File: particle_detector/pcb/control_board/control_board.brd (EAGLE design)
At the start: 64 x 32 mm, 35 parts, among them IC1 LT1807R, IC2 TLV3501, IC3 LT3461, IC4 TEENSY 3.2

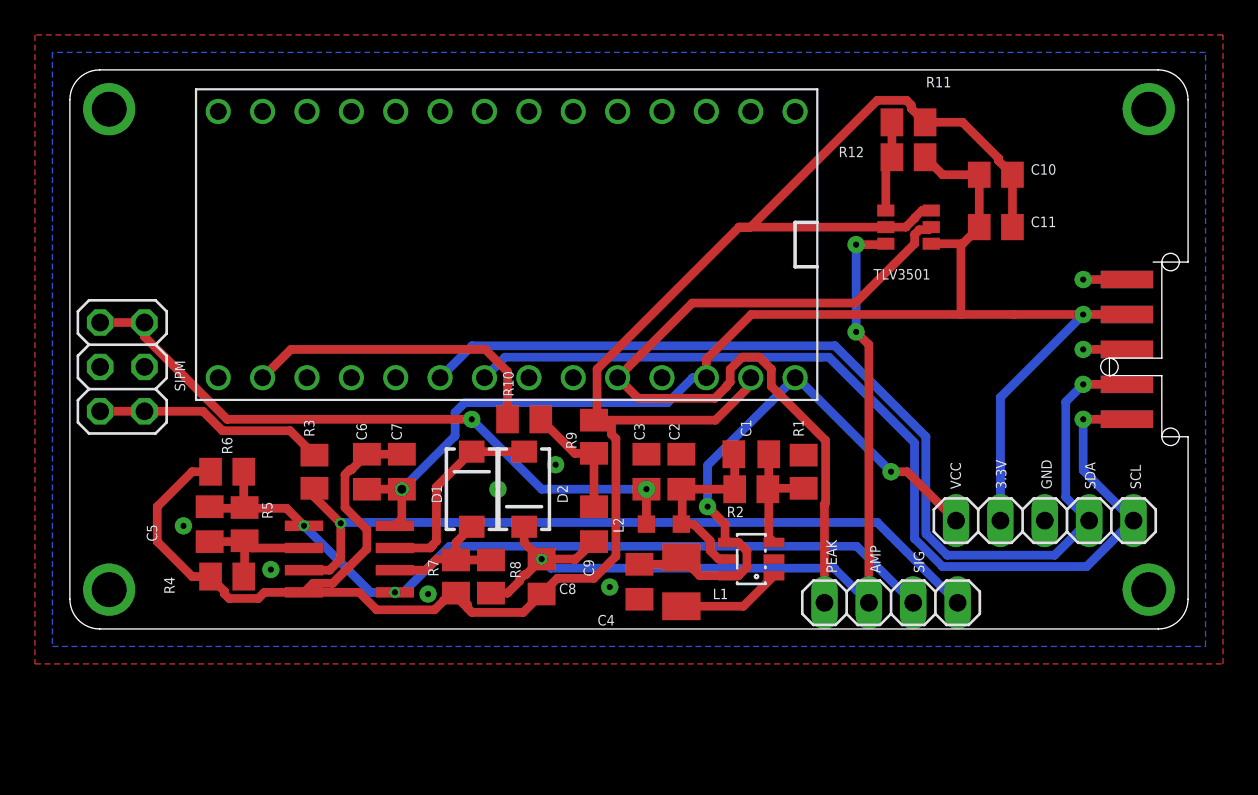
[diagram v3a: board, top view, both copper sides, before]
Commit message: remove VCC traces to DC-DC booster; 3.3V traces remain unrouted
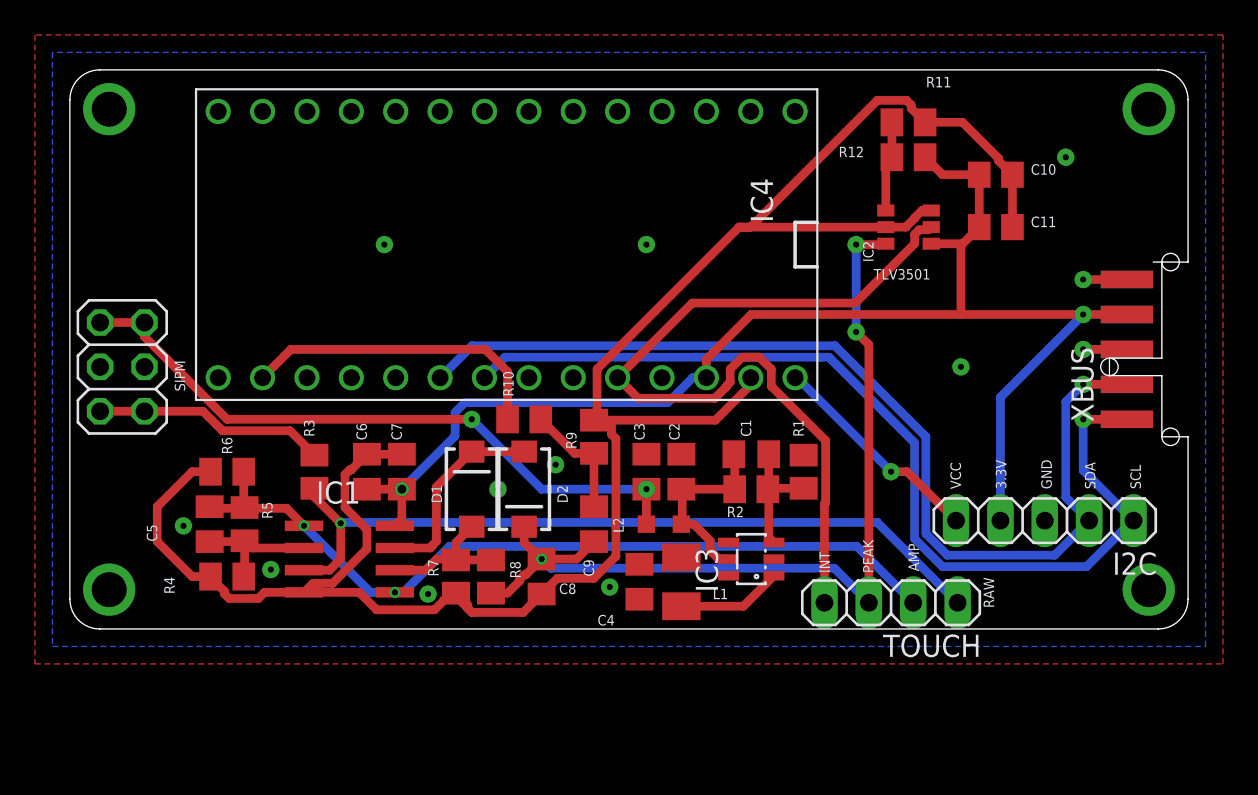
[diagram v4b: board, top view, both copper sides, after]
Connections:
- net 3.3V: now also C4.1, IC3.4, IC3.6, L1.1
- net VCC: no longer C4.1, IC3.4, IC3.6, L1.1
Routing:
- net VCC: track 33.7 -> 12.6 mm, vias 2 -> 1
- net 3.3V: track 78.8 -> 79.4 mm
- net GND: vias 11 -> 15
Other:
- board text added: "INT"
- board text added: "RAW"
- board text removed: "SIG"

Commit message: adjust comparator footprint; route 3.3V traces. send to fab
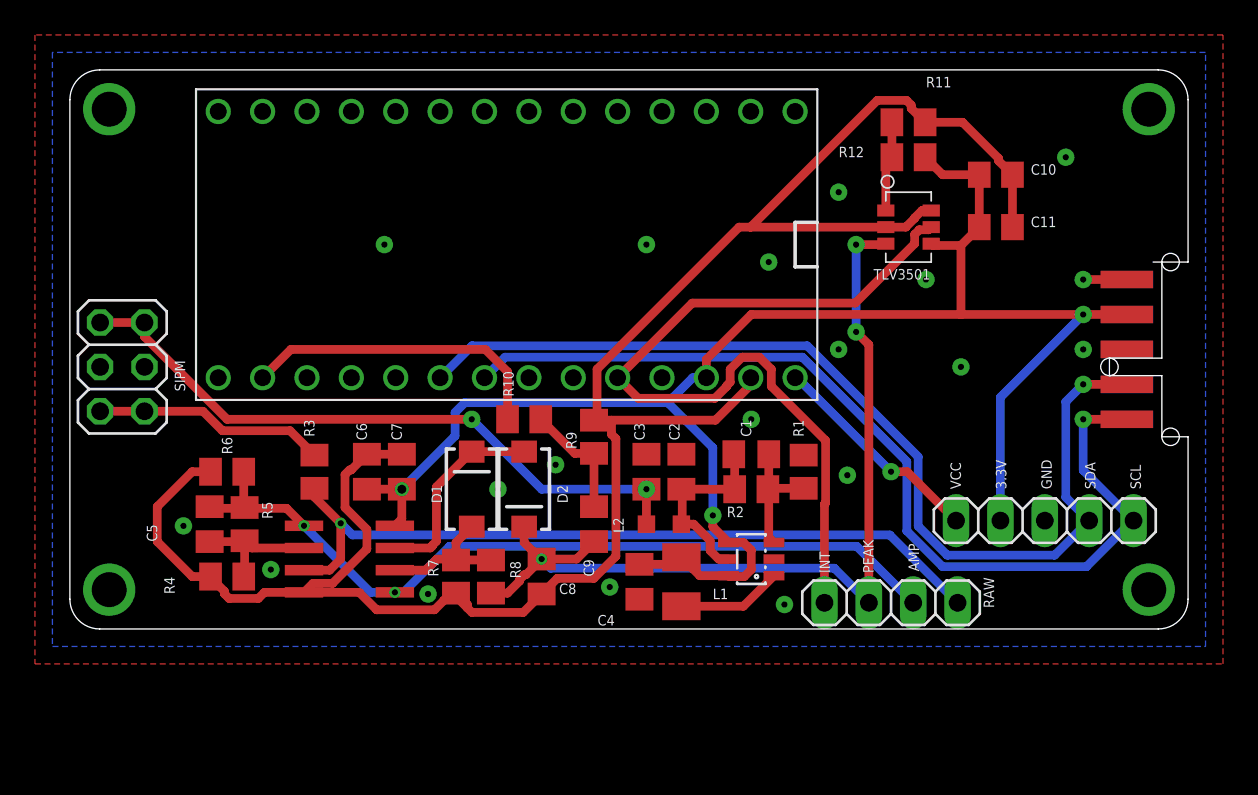
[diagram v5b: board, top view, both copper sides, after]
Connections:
- net 3.3V: now also XBUS.VCC; no longer XBUS.4
- net GND: now also XBUS.GND; no longer XBUS.3
- net SCL: now also XBUS.SCL; no longer XBUS.1
- net SDA: now also XBUS.SDA; no longer XBUS.2
- net VBAT: now also XBUS.VBAT; no longer XBUS.5
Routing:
- net 3.3V: track 79.4 -> 98.0 mm, vias 2 -> 3
- net GND: track 2.50 -> 0.00 mm, vias 15 -> 22
- net AGND: track 118.9 -> 117.6 mm
- net SDA: track 58.2 -> 57.3 mm
- net SCL: track 56.4 -> 55.5 mm

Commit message: begin fix of INT section
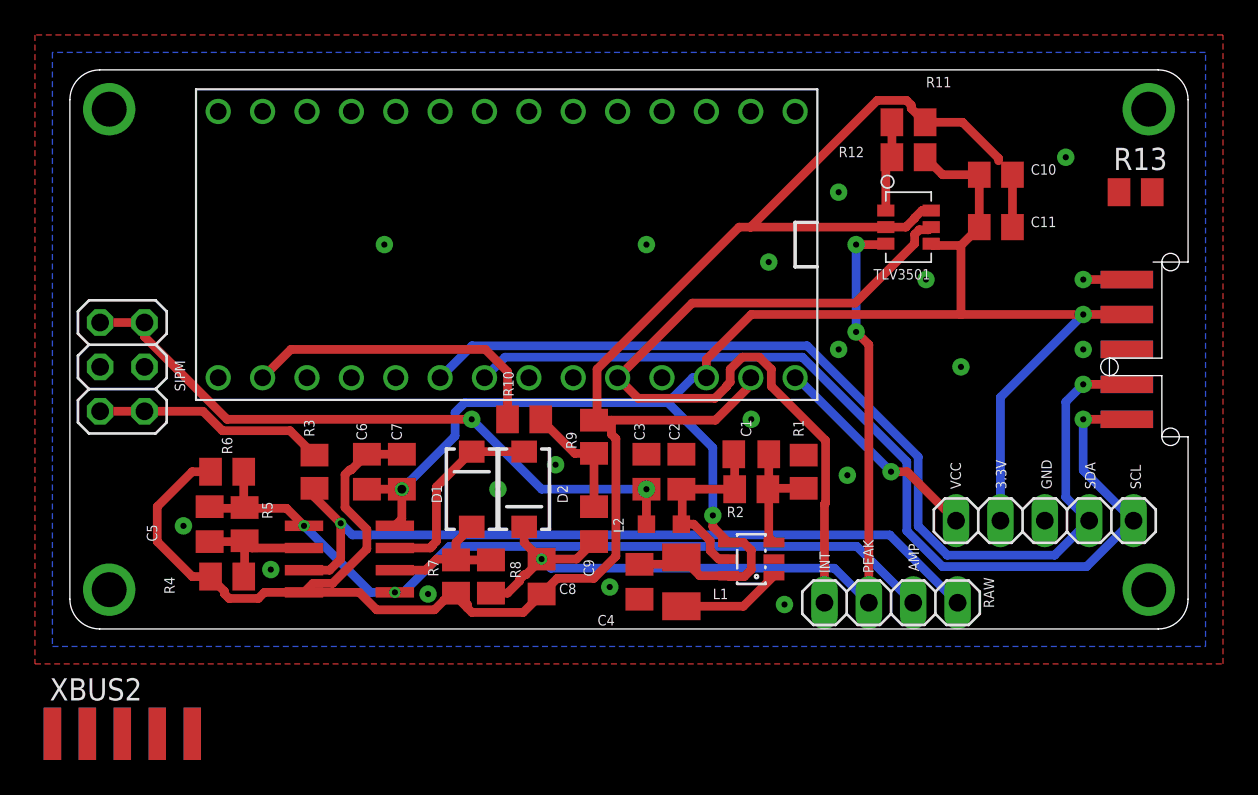
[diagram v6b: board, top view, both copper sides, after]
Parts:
- added R13: 47, resistor:M0805
- added XBUS2: (no value), personal:XBUS_2X05_PAD
- C10: value 10uF -> 0.1uF
- C11: value 0.1uF -> 2.2uF
- R11: value 1k -> 47
- R12: value 100k -> 470
- renumbered XBUS to XBUS1
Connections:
- net 3.3V: now also XBUS2.VCC
- net AGND: no longer C10.2, C11.2
- net GND: now also C10.2, C11.2, R13.1, XBUS2.GND
- net SCL: now also XBUS2.SCL
- net SDA: now also XBUS2.SDA
- net SIG_AMP: now also IC2.P$3
- net SIG_INT: now also R13.2
- net SIG_PEAK: no longer IC2.P$3
- net VBAT: now also XBUS2.VBAT
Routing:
- net AGND: track 117.6 -> 113.5 mm
- net GND: track 0.00 -> 3.00 mm
